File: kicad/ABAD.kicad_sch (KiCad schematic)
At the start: 62 parts, among them J1 Edge mounted SMA, J2 USB_C_Receptacle_USB2.0_16P, J3 BATT Screw Terminal, Q1 AO3401A, Q2 AO3401A, U2 ESP32-S3-WROOM-1, U3 USBLC6-2SC6, U4 TPS63001, U5 SAM-M8Q, U6 MPU-6050, U7 MS5611-01BA

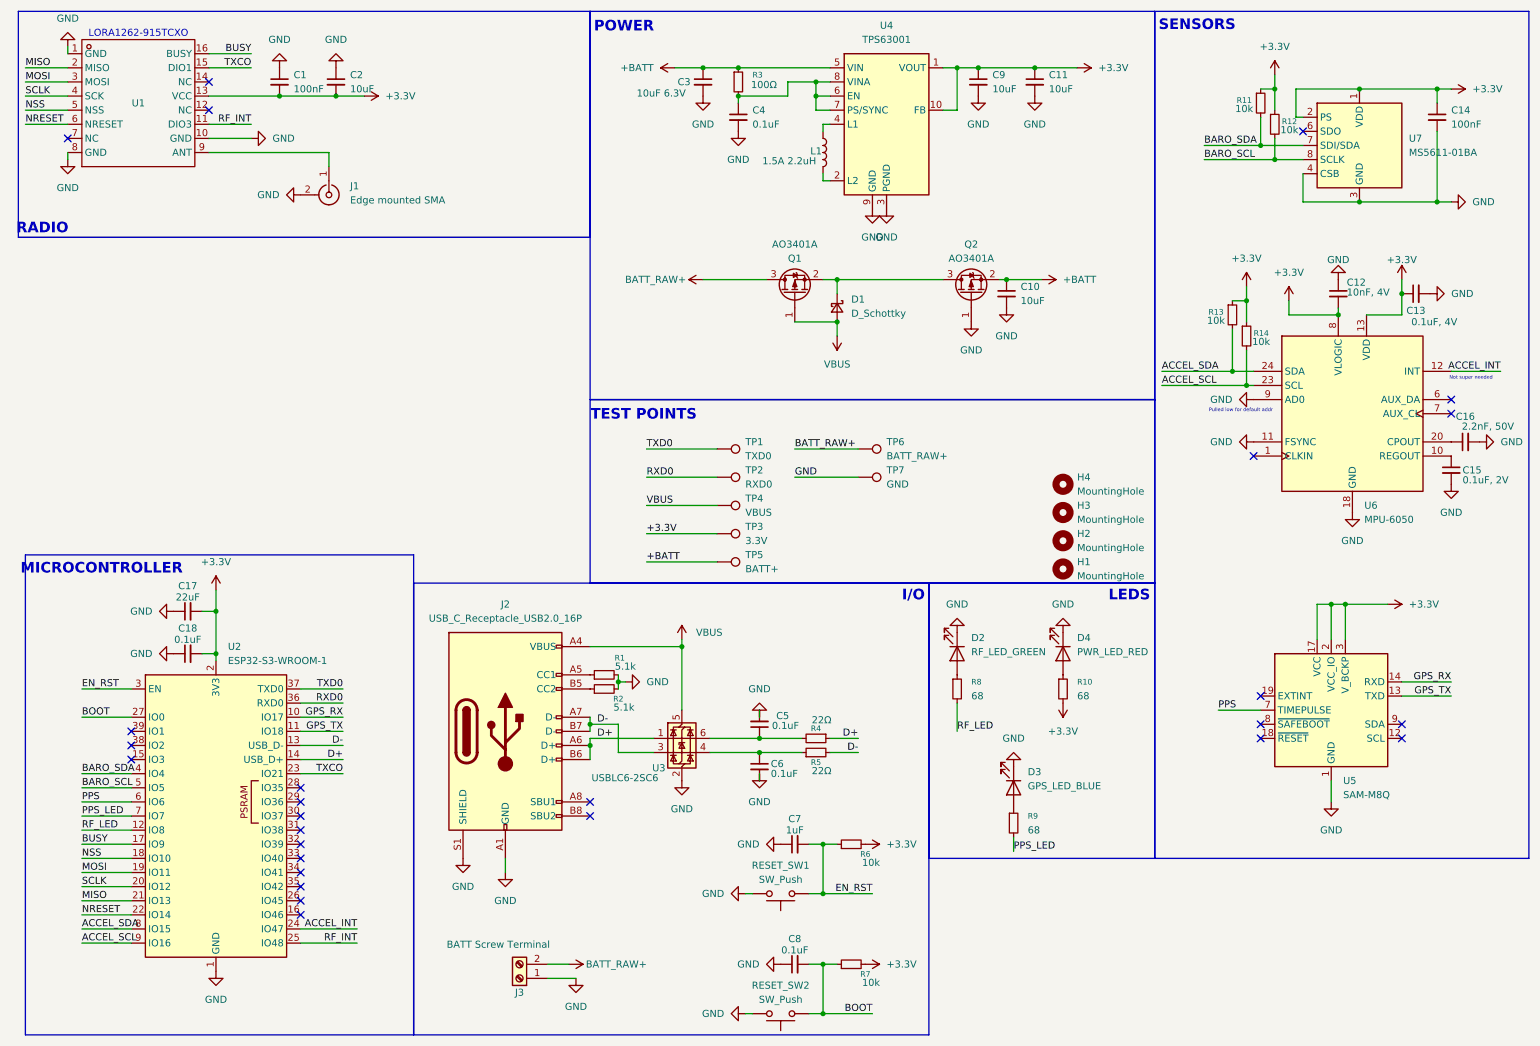
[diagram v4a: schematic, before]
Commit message: ESD array and Net labels fixed
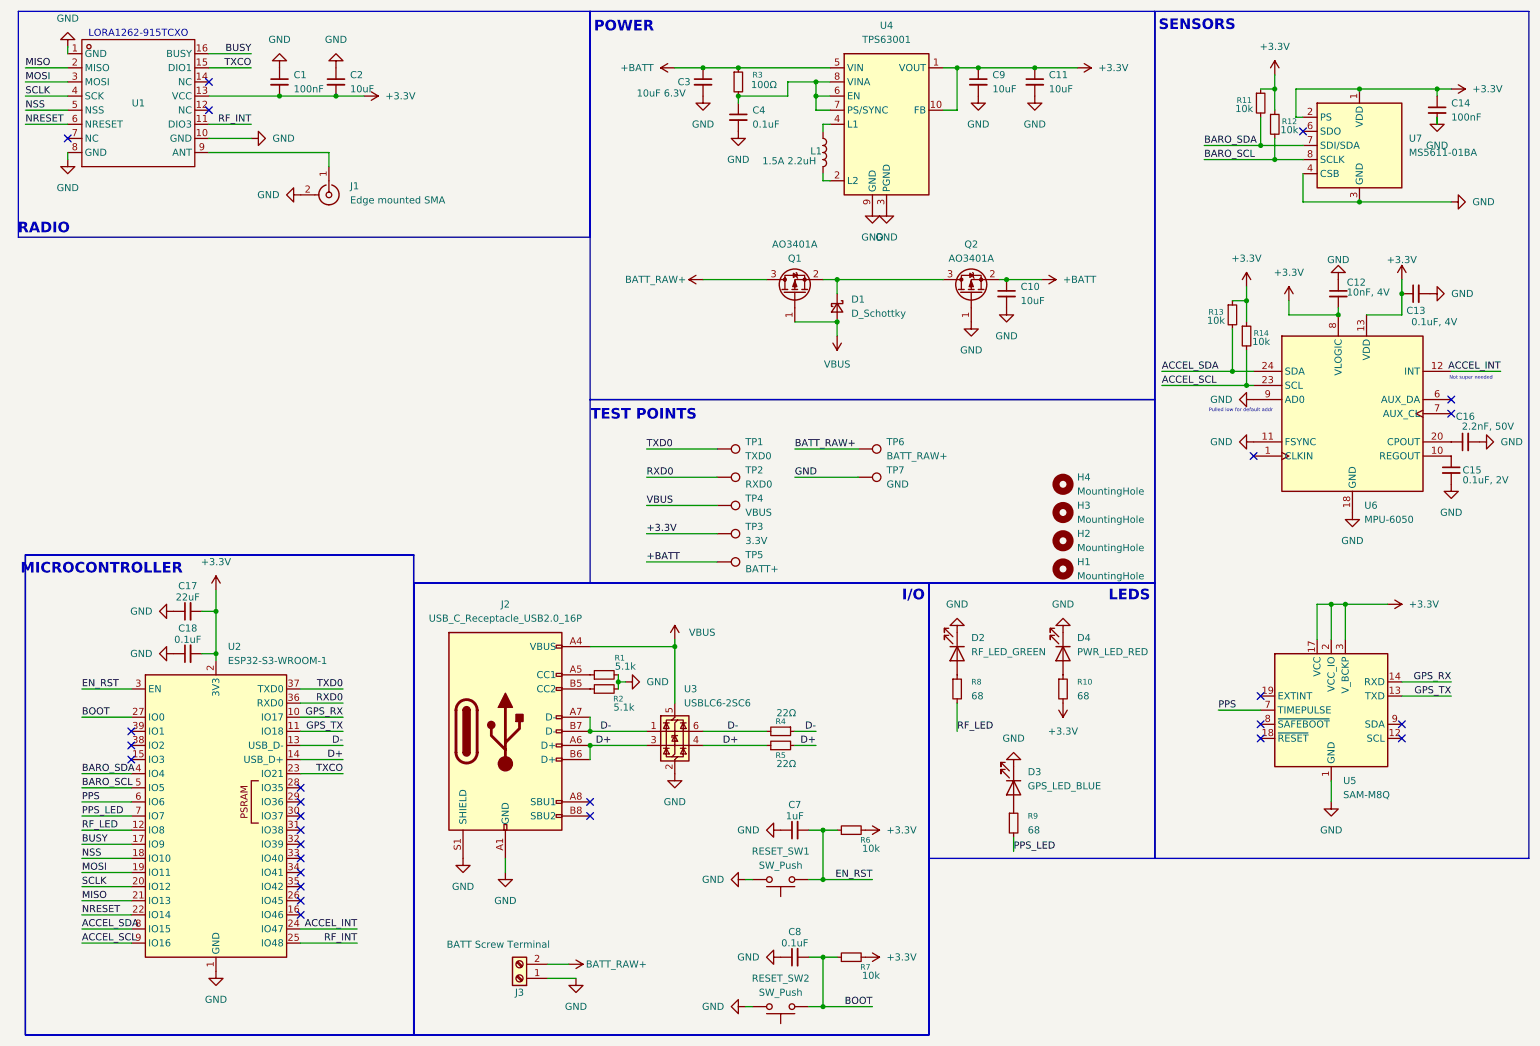
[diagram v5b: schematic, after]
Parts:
- removed C5, C6: 0.1uF, Capacitor_SMD:C_0805_2012Metric, symbol Device:C_Small
- H1, H2, H3, H4: footprint MountingHole:MountingHole_3.2mm_M3 -> MountingHole:MountingHole_3.2mm_M3_Pad
- J2: footprint Connector_USB:USB_Micro-B_Wuerth_629105150521_CircularHoles -> Connector_USB:USB_C_Receptacle_GCT_USB4105-xx-A_16P_TopMnt_Horizontal
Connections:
- net D+: now also R5.1, R5.2, U3.3 (I/O2), U3.4 (I/O2); no longer R4.1, U3.1 (I/O1)
- net D-: now also R4.1, R4.2, U3.1 (I/O1), U3.6 (I/O1); no longer R5.2, U3.3 (I/O2)
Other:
- moved on the sheet: C14, C7, C8, R4, R5, R6, R7, RESET_SW1, RESET_SW2

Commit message: 4 layer PCB design - now deprecated due to high production cost
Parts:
- removed H3, H4: MountingHole, MountingHole:MountingHole_3.2mm_M3_Pad, symbol Mechanical:MountingHole
- removed U5: SAM-M8Q, RF_GPS:ublox_SAM-M8Q, symbol RF_GPS:SAM-M8Q
- added U8: L80-R, RF_GPS:Quectel_L80-R, symbol RF_GPS:L80-R
- U1: footprint Lora1262_915TXCO:WIRELM-SMD_16P-L16.0-W16.0-P2.00_LORA-CC68-915MHZ-TCXO -> Lora1262:WIRELM-SMD_16P-L16.0-W16.0-P2.00_LORA-CC68-915MHZ-TCXO
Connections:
- net +3.3V: now also U8.4 (VCC), U8.5 (V_BCKP)
- net GND: now also U8.12 (GND), U8.3 (GND)
- net GPS_RX: now also U8.1 (RXD1)
- net GPS_TX: now also U8.2 (TXD1)
- net PPS: now also U8.6 (1PPS)
- removed net D+: J2.A6 (D+), J2.B6 (D+), R5.1, R5.2, U2.14 (USB_D+), U3.3 (I/O2), U3.4 (I/O2)
- removed net D-: J2.A7 (D-), J2.B7 (D-), R4.1, R4.2, U2.13 (USB_D-), U3.1 (I/O1), U3.6 (I/O1)
- new net: R4.2, U3.6 (I/O1)
- new net: R5.1, U3.4 (I/O2)
- new net USB+: J2.A6 (D+), J2.B6 (D+), U3.3 (I/O2)
- new net USB-: J2.A7 (D-), J2.B7 (D-), U3.1 (I/O1)
- new net USBN: R4.1, U2.13 (USB_D-)
- new net USBP: R5.2, U2.14 (USB_D+)
- no-connect marks 27 -> 26
